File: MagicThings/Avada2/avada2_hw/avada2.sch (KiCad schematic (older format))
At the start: 34 parts

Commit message: 
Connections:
- wire segments 116 -> 117
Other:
- moved on the sheet: C?, D?, L?, R?

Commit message: 
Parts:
- added C?: 4.7u, symbol C
- added C?: 1u, symbol C
- added D?: BZV55-C24, symbol ZENER
- added D? (x2): LED, symbol LED
- added D?: BAT54WS, symbol D_SHOTTKY
- added DA?: LT1932, symbol LT1932
- added L? (x2): 6.8uH, symbol L
- added R?: 1.2k, symbol R
- added XL? (x3): CONN_1, symbol CONN_1
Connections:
- net labels added: In, LOut, LedLow, Out
- wire segments 117 -> 145
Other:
- note added: "+BATTERY"
- note added: "-BATTERY"
- note added: "1.2k =>18mA"
- note added: "Inductors of different packages"
- note added: "LEDs of\ndifferent\npackages"
- note added: "ZENER for overvoltage\nprotection in case of\nopen circuit"
- moved on the sheet: BZ?, C?, D?, DA?, DD?, L?, Q?, R?, SW?

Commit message: Avada2 sch done
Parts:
- removed B?: BAT, BAT_LP383450, symbol BAT
- removed D?: BZV55-C24, symbol ZENER
- removed D? (x2): LED, symbol LED
- removed DA?: LT1932, symbol LT1932
- removed L? (x2): 6.8uH, symbol L
- removed R?: 5.1k, RES_0603, symbol R
- removed R?: 10k, RES_0603, symbol R
- removed R?: R, RES_0603, symbol R
- removed R?: 1.2k, symbol R
- removed SW?: BUTTON, symbol BUTTON
- removed XL? (x3): CONN_1, symbol CONN_1
- added C11, C12, C13: 10u, CAP_0805, symbol C
- added D2: LED, symbol LED
- added D5: BAT54WS, symbol D_SHOTTKY
- added F1: FUSE0R, symbol FUSE0R
- added HOLE1, HOLE2: HOLE_METALLED, symbol HOLE_METALLED
- added L1: 100uH, IND_1812, symbol L
- added Q1, Q2: MMBT2222, symbol NPN
- added R1, R3: 1k, RES_0603, symbol R
- added R12, R13, R14, R4, R5, R6, R7: R*, RES_0805, symbol R
- added R2: 100R, RES_0603, symbol R
- added SW4, SW5: BUTTON_H, symbol BUTTON_H
- added SW6: SWITCH, symbol SWITCH
- added XL2, XL3: CONN_1, symbol CONN_1
- C10: renamed from C?; value 4.7uF -> 10u; footprint CAP_0603 -> CAP_0805
- C14: renamed from C?; value 10nF -> 10n
- C9: renamed from C?; value 2.2uF -> 4.7u
- D3: renamed from D?; value D_SHOTTKY -> SS14
- L2: renamed from L?; footprint IND_1812 -> IND603
- R11: renamed from R?; value R -> R*; footprint RES_0603 -> RES_0805
- R15, R16: renamed from R?; value 100k -> 390k
- gave numbers to parts that had none: 24
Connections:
- net labels added: Batt, BckLtEnable, Bck_mid, Btn5, Emitter, Green_Light, L_low, LedHigh, Led_a, Led_c
- net labels removed: In, LOut, Out
- wire segments 145 -> 176
- no-connect marks 7 -> 25
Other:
- note added: "Xotar Led"
- note removed: "+BATTERY"
- note removed: "-BATTERY"
- note removed: "1.2k =>18mA"
- note removed: "Inductors of different packages"
- note removed: "LEDs of\ndifferent\npackages"
- note removed: "ZENER for overvoltage\nprotection in case of\nopen circuit"
- moved on the sheet: C1, C10, C14, C2, C9, D4, DA1, L2, R10, R11

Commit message: 
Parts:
- removed D5: BAT54WS, symbol D_SHOTTKY
- added XL?: ST_SWD, symbol ST_SWD
- added XL?: CONN_2, symbol CONN_2
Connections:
- net labels added: SWCLK, SWDIO, TX1
- wire segments 176 -> 183
- no-connect marks 25 -> 22
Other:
- note added: "Programming"
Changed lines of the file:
@@
-EESchema Schematic File Version 2  date 06/12/2012 00:38:38
+EESchema Schematic File Version 2  date 06/12/2012 14:48:30
 LIBS:Transistors_kl
 LIBS:Connectors_kl
@@
 Sheet 1 1
 Title ""
-Date "5 dec 2012"
+Date "6 dec 2012"
 Rev ""
 Comp ""
@@
 $EndDescr
 Wire Wire Line
+	12900 3050 13850 3050
+Wire Wire Line
+	12900 3050 12900 2550
+Wire Wire Line
+	13850 3250 13800 3250
+Wire Wire Line
+	12250 3050 12350 3050
+Wire Wire Line
+	12350 2950 12250 2950
+Wire Wire Line
+	1800 5200 1700 5200
+Wire Wire Line
+	1850 5450 1850 5400
+Wire Wire Line
+	1850 5400 1700 5400
+Wire Wire Line
+	1700 5300 1850 5300
+Wire Wire Line
+	1700 5100 1800 5100
+Wire Wire Line
 	14000 2400 14000 2350
 Connection ~ 14250 8950
 Wire Wire Line
 	14150 8950 14250 8950
-Connection ~ 14350 6900
-Wire Wire Line
-	14350 6900 14350 6650
-Wire Wire Line
-	14350 6650 14450 6650
 Connection ~ 9700 10200
 Wire Wire Line
@@
 	9700 9650 9500 9650
 Wire Wire Line
-	14850 6650 14950 6650
-Wire Wire Line
-	14950 6650 14950 6900
-Connection ~ 14950 6900
-Wire Wire Line
 	14250 9150 14250 8700
 Wire Wire Line
@@
 Wire Wire Line
 	14000 2700 14000 2650
+Wire Wire Line
+	12900 2550 12250 2550
+$Comp
+L CONN_2 XL?
+U 1 1 50C077CC
+P 14050 3150
+F 0 "XL?" V 14000 3150 40  0000 C CNN
+F 1 "CONN_2" V 14100 3150 40  0000 C CNN
+	1    14050 3150
+	1    0    0    -1
+$EndComp
+Text Label 13300 3050 0    60   ~ 0
+TX1
+$Comp
+L GND #PWR?
+U 1 1 50C077B8
+P 13800 3250
+F 0 "#PWR?" H 13890 3230 30  0001 C CNN
+F 1 "GND" H 13800 3170 30  0001 C CNN
+	1    13800 3250
+	0    -1   -1   0
+$EndComp
+Text Label 12350 3050 0    60   ~ 0
+SWCLK
+Text Label 12350 2950 0    60   ~ 0
+SWDIO
+Text Notes 1150 4800 0    60   ~ 0
+Programming
+Text Label 1800 5200 0    60   ~ 0
+SWDIO
+Text Label 1800 5100 0    60   ~ 0
+SWCLK
+$Comp
+L ST_SWD XL?
+U 1 1 50C07760
+P 1350 5250
+F 0 "XL?" H 1200 5550 60  0000 C CNN
+F 1 "ST_SWD" H 1550 5550 60  0000 C CNN
+	1    1350 5250
+	1    0    0    -1
+$EndComp
+$Comp
+L GND #PWR?
+U 1 1 50C0775F
+P 1850 5450
+F 0 "#PWR?" H 1940 5430 30  0001 C CNN
+F 1 "GND" H 1850 5370 30  0001 C CNN
+	1    1850 5450
+	1    0    0    -1
+$EndComp
+$Comp
+L +3.3V #PWR?
+U 1 1 50C0775E
+P 1850 5300
+F 0 "#PWR?" H 1850 5260 30  0001 C CNN
+F 1 "+3.3V" H 1930 5330 30  0000 C CNN
+	1    1850 5300
+	1    0    0    -1
+$EndComp
 $Comp
 L BUTTON_H SW5
@@
 F 1 "HOLE_METALLED" H 13300 8750 60  0000 C CNN
 	1    13850 8700
-	1    0    0    -1
-$EndComp
-$Comp
-L D_SHOTTKY D5
-U 1 1 50BFAA0E
-P 14650 6650
-F 0 "D5" H 14650 6750 40  0000 C CNN
-F 1 "BAT54WS" H 14650 6550 40  0000 C CNN
-	1    14650 6650
 	1    0    0    -1
 $EndComp
@@
 NoConn ~ 12250 2250
 NoConn ~ 12250 2350
-NoConn ~ 12250 2550
 NoConn ~ 12250 2650
 NoConn ~ 12250 2750
 NoConn ~ 12250 2850
-NoConn ~ 12250 2950
-NoConn ~ 12250 3050
 NoConn ~ 12250 3150
 NoConn ~ 12250 3650

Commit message: 
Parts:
- removed D4: LED, symbol LED
- added D4: LED_RAD, symbol LED_RAD
- gave numbers to parts that had none: 2
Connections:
- no-connect marks 22 -> 23

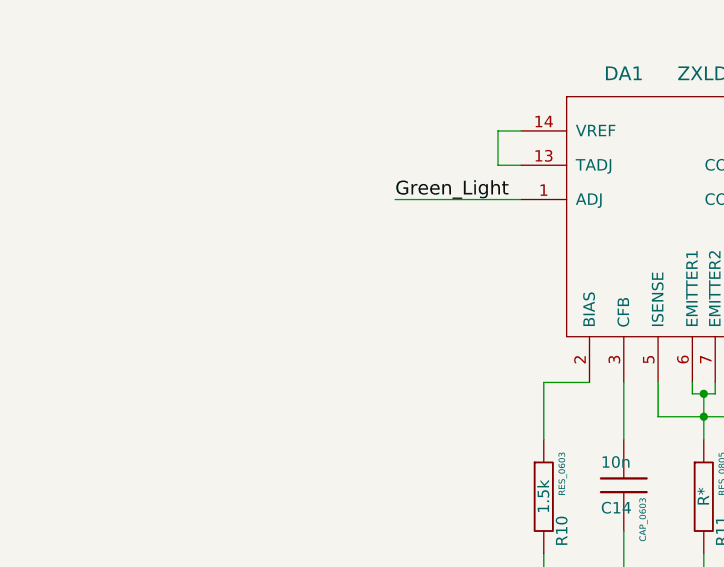
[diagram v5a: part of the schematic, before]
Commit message: Flash and Buzz completed. + Resistor to eliminate power-on flash
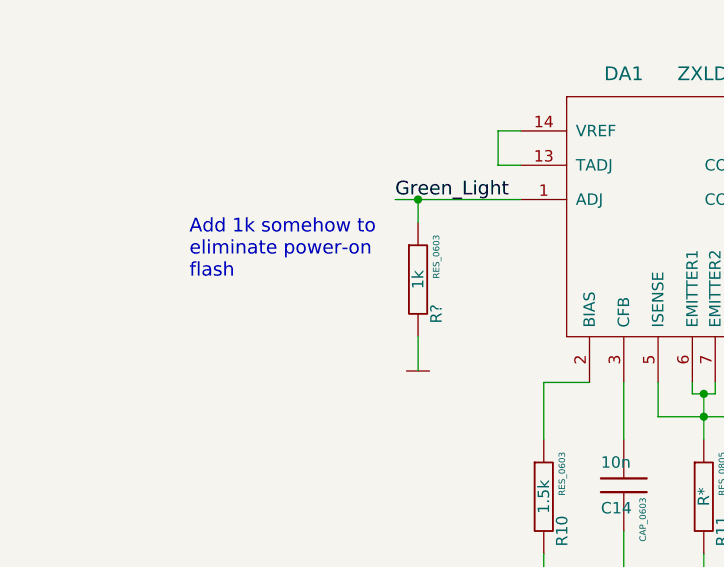
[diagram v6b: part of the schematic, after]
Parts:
- added R?: 1k, RES_0603, symbol R
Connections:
- wire segments 183 -> 185
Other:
- note added: "Add 1k somehow to \neliminate power-on \nflash"
